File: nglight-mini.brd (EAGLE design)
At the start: 15.5 x 19.3 mm, 25 parts

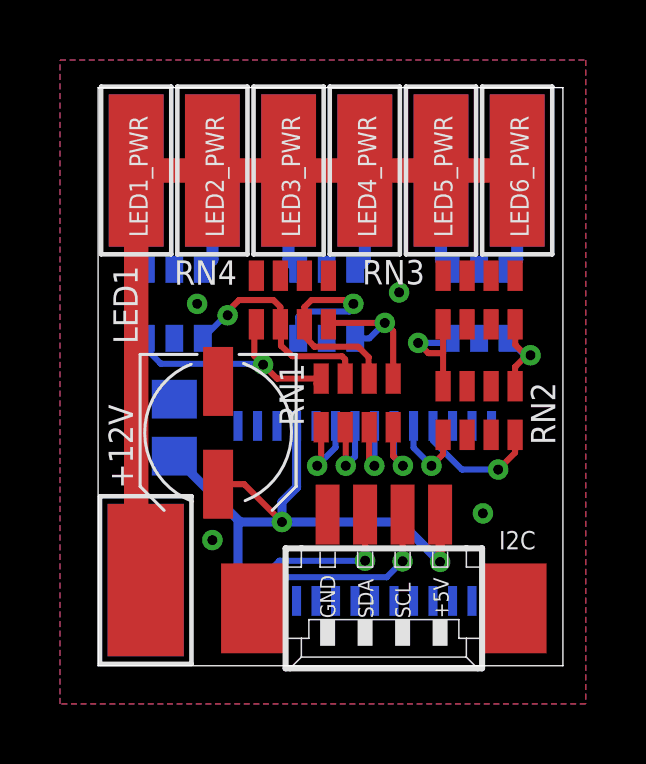
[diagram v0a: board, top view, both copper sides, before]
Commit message: Minor trace/via adjustments
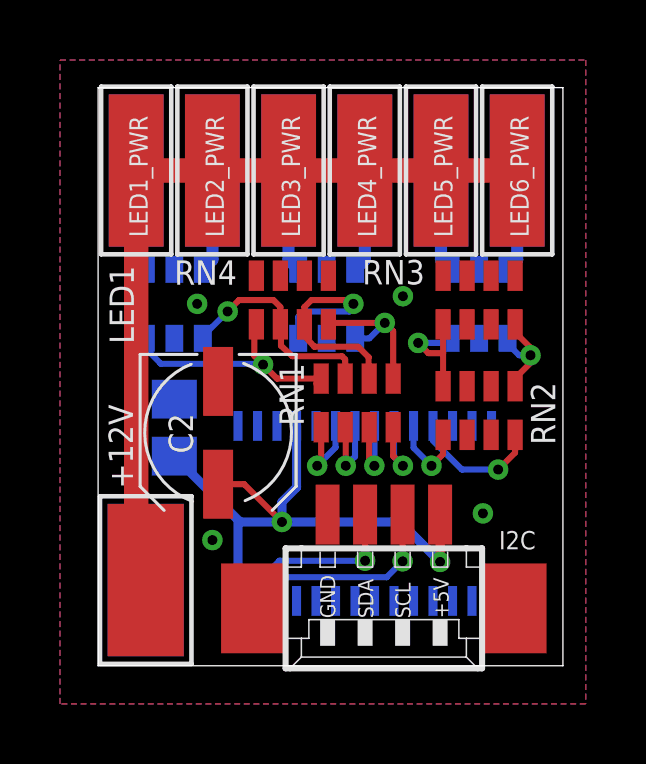
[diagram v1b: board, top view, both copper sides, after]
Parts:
- C1: value (none) -> 100n
- C2: value (none) -> 10uF
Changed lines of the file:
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@@
 <grid distance="5" unitdist="mil" unit="mil" style="lines" multiple="1" display="no" altdistance="1.25" altunitdist="mil" altunit="mil"/>
 <layers>
-<layer number="1" name="Top" color="4" fill="1" visible="yes" active="yes"/>
+<layer number="1" name="Top" color="4" fill="1" visible="no" active="yes"/>
 <layer number="2" name="Route2" color="1" fill="3" visible="no" active="no"/>
 <layer number="3" name="Route3" color="4" fill="3" visible="no" active="no"/>
@@
 <layer number="19" name="Unrouted" color="6" fill="1" visible="yes" active="yes"/>
 <layer number="20" name="Dimension" color="15" fill="1" visible="yes" active="yes"/>
-<layer number="21" name="tPlace" color="7" fill="1" visible="yes" active="yes"/>
+<layer number="21" name="tPlace" color="7" fill="1" visible="no" active="yes"/>
 <layer number="22" name="bPlace" color="7" fill="1" visible="yes" active="yes"/>
-<layer number="23" name="tOrigins" color="15" fill="1" visible="yes" active="yes"/>
+<layer number="23" name="tOrigins" color="15" fill="1" visible="no" active="yes"/>
 <layer number="24" name="bOrigins" color="15" fill="1" visible="yes" active="yes"/>
-<layer number="25" name="tNames" color="7" fill="1" visible="yes" active="yes"/>
+<layer number="25" name="tNames" color="7" fill="1" visible="no" active="yes"/>
 <layer number="26" name="bNames" color="7" fill="1" visible="yes" active="yes"/>
-<layer number="27" name="tValues" color="7" fill="1" visible="yes" active="yes"/>
+<layer number="27" name="tValues" color="7" fill="1" visible="no" active="yes"/>
 <layer number="28" name="bValues" color="7" fill="1" visible="yes" active="yes"/>
-<layer number="29" name="tStop" color="7" fill="3" visible="yes" active="yes"/>
+<layer number="29" name="tStop" color="7" fill="3" visible="no" active="yes"/>
 <layer number="30" name="bStop" color="7" fill="6" visible="yes" active="yes"/>
-<layer number="31" name="tCream" color="7" fill="4" visible="yes" active="yes"/>
+<layer number="31" name="tCream" color="7" fill="4" visible="no" active="yes"/>
 <layer number="32" name="bCream" color="7" fill="5" visible="yes" active="yes"/>
-<layer number="33" name="tFinish" color="6" fill="3" visible="yes" active="yes"/>
+<layer number="33" name="tFinish" color="6" fill="3" visible="no" active="yes"/>
 <layer number="34" name="bFinish" color="6" fill="6" visible="yes" active="yes"/>
-<layer number="35" name="tGlue" color="7" fill="4" visible="yes" active="yes"/>
+<layer number="35" name="tGlue" color="7" fill="4" visible="no" active="yes"/>
 <layer number="36" name="bGlue" color="7" fill="5" visible="yes" active="yes"/>
 <layer number="37" name="tTest" color="7" fill="1" visible="yes" active="yes"/>
 <layer number="38" name="bTest" color="7" fill="1" visible="yes" active="yes"/>
-<layer number="39" name="tKeepout" color="4" fill="11" visible="yes" active="yes"/>
+<layer number="39" name="tKeepout" color="4" fill="11" visible="no" active="yes"/>
 <layer number="40" name="bKeepout" color="1" fill="11" visible="yes" active="yes"/>
-<layer number="41" name="tRestrict" color="4" fill="10" visible="yes" active="yes"/>
+<layer number="41" name="tRestrict" color="4" fill="10" visible="no" active="yes"/>
 <layer number="42" name="bRestrict" color="1" fill="10" visible="yes" active="yes"/>
 <layer number="43" name="vRestrict" color="2" fill="10" visible="yes" active="yes"/>
@@
 <layer number="49" name="Reference" color="7" fill="1" visible="yes" active="yes"/>
 <layer number="50" name="dxf" color="7" fill="1" visible="no" active="no"/>
-<layer number="51" name="tDocu" color="7" fill="1" visible="yes" active="yes"/>
+<layer number="51" name="tDocu" color="7" fill="1" visible="no" active="yes"/>
 <layer number="52" name="bDocu" color="7" fill="1" visible="yes" active="yes"/>
 <layer number="53" name="tGND_GNDA" color="7" fill="9" visible="no" active="no"/>
@@
 <wire x1="15.494" y1="19.27225" x2="0" y2="19.27225" width="0" layer="20"/>
 <wire x1="0" y1="19.27225" x2="0" y2="0" width="0" layer="20"/>
-<text x="14.82725" y="8.66775" size="0.8128" layer="26" rot="MR270">nglight-mini r1</text>
-<text x="0.508" y="13.335" size="0.8128" layer="25" rot="R270">LED1</text>
+<text x="14.95425" y="9.68375" size="1.016" layer="26" rot="MR270">nglight-mini r1</text>
+<text x="0.381" y="13.335" size="0.8128" layer="25" rot="R270">LED1</text>
 <polygon width="0.3048" layer="41">
 <vertex x="0.3175" y="19.05"/>
@@
 <attribute name="VALUE" x="3.71" y="19.31" size="0.0254" layer="27"/>
 </element>
-<element name="C1" library="rcl" package="C0805" value="" x="2.54" y="7.9375" smashed="yes" rot="MR90">
-<attribute name="NAME" x="4.28625" y="9.4615" size="0.8128" layer="26" rot="MR270"/>
-<attribute name="VALUE" x="0" y="6.6675" size="1.27" layer="28" rot="MR90"/>
-</element>
-<element name="C2" library="rcl" package="UD-5X5,8_NICHICON" value="" x="4.0005" y="7.77875" smashed="yes" rot="R270">
-<attribute name="VALUE" x="1.4605" y="9.04875" size="1.27" layer="27" rot="R270"/>
+<element name="C1" library="rcl" package="C0805" value="100n" x="2.54" y="7.9375" smashed="yes" rot="MR90">
+<attribute name="NAME" x="3.4925" y="9.62025" size="0.8128" layer="26" rot="MR180"/>
+<attribute name="VALUE" x="3.556" y="6.5405" size="0.6096" layer="28" rot="MR90"/>
+</element>
+<element name="C2" library="rcl" package="UD-5X5,8_NICHICON" value="10uF" x="4.0005" y="7.77875" smashed="yes" rot="R270">
+<attribute name="NAME" x="2.3495" y="8.41375" size="0.8128" layer="25" rot="R270"/>
+<attribute name="VALUE" x="4.8895" y="8.92175" size="0.8128" layer="27" rot="R270"/>
 </element>
 <element name="+12V" library="wirepad" package="5-2,5" value="WIREPADSMD5-2,5" x="1.5875" y="2.8575" smashed="yes">
@@
 <element name="Q1" library="dualfet" package="SOT23-6" value="" x="12.7" y="12.065" smashed="yes" rot="MR0">
 <attribute name="VALUE" x="14.097" y="9.393" size="1.016" layer="28" ratio="10" rot="MR0"/>
-<attribute name="NAME" x="14.529" y="11.176" size="0.8128" layer="26" ratio="10" rot="MR90"/>
+<attribute name="NAME" x="14.275" y="11.303" size="0.8128" layer="26" ratio="10" rot="MR90"/>
 </element>
 <element name="Q2" library="dualfet" package="SOT23-6" value="" x="7.62" y="12.065" smashed="yes" rot="MR0">
 <attribute name="VALUE" x="9.017" y="9.393" size="1.016" layer="28" ratio="10" rot="MR0"/>
-<attribute name="NAME" x="5.791" y="12.954" size="0.8128" layer="26" ratio="10" rot="MR270"/>
+<attribute name="NAME" x="6.045" y="12.7" size="0.8128" layer="26" ratio="10" rot="MR270"/>
 </element>
 <element name="Q3" library="dualfet" package="SOT23-6" value="" x="2.54" y="12.065" smashed="yes" rot="MR0">
@@
 <contactref element="RN3" pad="7"/>
 <via x="12.827" y="5.08" extent="1-16" drill="0.3302"/>
-<via x="10.033" y="12.446" extent="1-16" drill="0.3302"/>
+<via x="10.16" y="12.319" extent="1-16" drill="0.3302"/>
 <via x="3.302" y="12.065" extent="1-16" drill="0.3302"/>
 <via x="3.81" y="4.191" extent="1-16" drill="0.3302"/>
@@
 <contactref element="RN2" pad="5"/>
 <via x="14.4145" y="10.3505" extent="1-16" drill="0.3302"/>
-<wire x1="13.9" y1="9.319" x2="13.9" y2="9.963" width="0.2032" layer="1"/>
-<wire x1="13.65" y1="10.915" x2="14.2145" y2="10.3505" width="0.2032" layer="16"/>
-<wire x1="14.2145" y1="10.3505" x2="14.4145" y2="10.3505" width="0.2032" layer="16"/>
-<wire x1="13.9" y1="9.963" x2="14.2875" y2="10.3505" width="0.2032" layer="1"/>
-<wire x1="14.2875" y1="10.3505" x2="14.4145" y2="10.3505" width="0.2032" layer="1"/>
-<wire x1="14.4145" y1="10.3505" x2="14.25575" y2="10.3505" width="0.2032" layer="1"/>
-<wire x1="14.25575" y1="10.3505" x2="13.9065" y2="10.69975" width="0.2032" layer="1"/>
-<wire x1="13.9065" y1="10.69975" x2="13.9065" y2="11.3755" width="0.2032" layer="1"/>
 <wire x1="13.9065" y1="11.3755" x2="13.9" y2="11.382" width="0.2032" layer="1"/>
+<wire x1="14.4145" y1="10.3505" x2="14.4145" y2="10.0965" width="0.2032" layer="1"/>
+<wire x1="14.4145" y1="10.0965" x2="13.9" y2="9.582" width="0.2032" layer="1"/>
+<wire x1="13.9" y1="9.582" x2="13.9" y2="9.319" width="0.2032" layer="1"/>
+<wire x1="14.4145" y1="10.3505" x2="14.4145" y2="10.6045" width="0.2032" layer="1"/>
+<wire x1="14.4145" y1="10.6045" x2="13.9" y2="11.119" width="0.2032" layer="1"/>
+<wire x1="13.9" y1="11.119" x2="13.9" y2="11.382" width="0.2032" layer="1"/>
+<wire x1="14.4145" y1="10.3505" x2="14.0335" y2="10.3505" width="0.2032" layer="16"/>
+<wire x1="14.0335" y1="10.3505" x2="13.65" y2="10.734" width="0.2032" layer="16"/>
+<wire x1="13.65" y1="10.734" x2="13.65" y2="10.915" width="0.2032" layer="16"/>
 </signal>
 <signal name="N$6">
@@
 <wire x1="6.096" y1="10.668" x2="6.096" y2="11.363" width="0.2032" layer="1"/>
 <wire x1="6.096" y1="11.363" x2="6.077" y2="11.382" width="0.1524" layer="1"/>
-<via x="4.318" y="11.684" extent="1-16" drill="0.3302"/>
 <wire x1="4.699" y1="12.192" x2="5.842" y2="12.192" width="0.2032" layer="1"/>
 <wire x1="5.842" y1="12.192" x2="6.077" y2="11.957" width="0.2032" layer="1"/>
 <wire x1="6.077" y1="11.957" x2="6.077" y2="11.382" width="0.2032" layer="1"/>
 <wire x1="4.699" y1="12.192" x2="4.318" y2="11.811" width="0.2032" layer="1"/>
-<wire x1="4.318" y1="11.811" x2="4.318" y2="11.684" width="0.2032" layer="1"/>
-<wire x1="4.318" y1="11.684" x2="4.259" y2="11.684" width="0.2032" layer="16"/>
-<wire x1="4.259" y1="11.684" x2="3.49" y2="10.915" width="0.2032" layer="16"/>
 <wire x1="8.128" y1="10.31875" x2="8.236" y2="10.21075" width="0.2032" layer="1"/>
 <wire x1="8.236" y1="10.21075" x2="8.236" y2="9.573" width="0.2032" layer="1"/>
+<via x="4.318" y="11.811" extent="1-16" drill="0.3302"/>
+<wire x1="4.318" y1="11.811" x2="3.49" y2="10.983" width="0.2032" layer="16"/>
+<wire x1="3.49" y1="10.983" x2="3.49" y2="10.915" width="0.2032" layer="16"/>
 </signal>
 <signal name="LED5">
